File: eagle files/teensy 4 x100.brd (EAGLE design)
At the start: 94.9 x 68.9 mm, 57 parts, among them IC2 LTV846S, IC3 LTV846S, IC4 74AHCT541A, IC5 74AHCT541A, IC6 LM358D, IC7 ULN2003AD

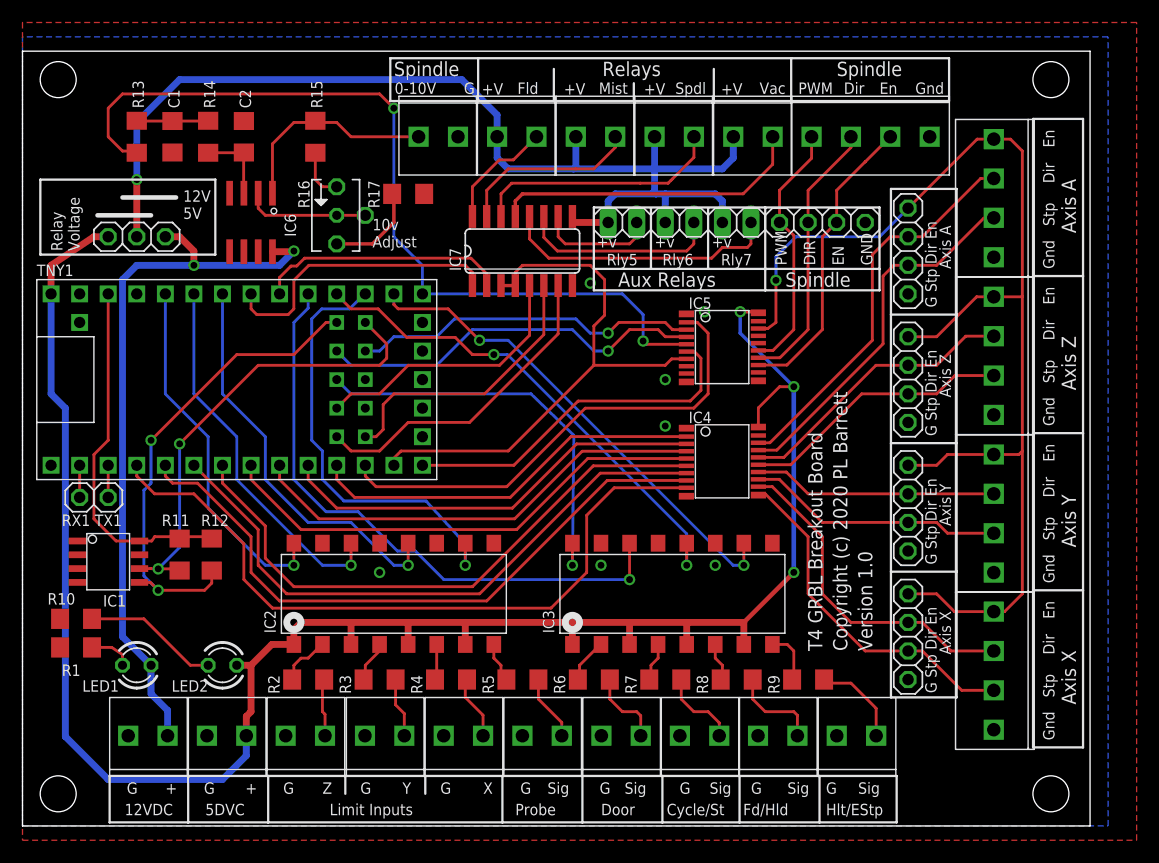
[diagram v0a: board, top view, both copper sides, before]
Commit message: Add files via upload
fix to stepper enable lines
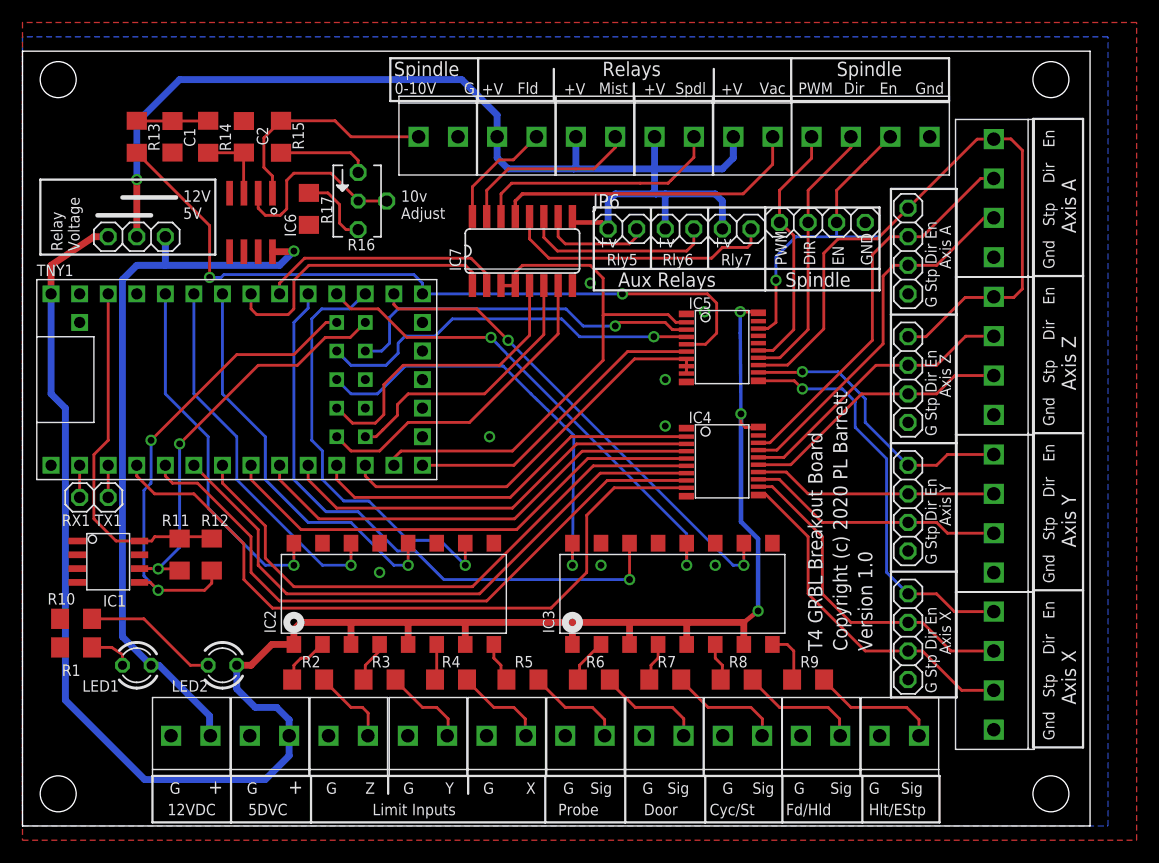
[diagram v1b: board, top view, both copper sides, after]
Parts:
- IC1: value (none) -> 24LCxxx
- JP6: device pinhead:1X06 -> phils connectors:1X06
- moved R17 8.93 mm to (25.5, 54.9), turned to 90 degrees
- moved TR10 3.81 mm to (29.0, 8.02)
- moved TR2 3.81 mm to (22.0, 8.02)
- moved TR5 3.81 mm to (64.0, 8.02)
- moved TR6 3.81 mm to (57.0, 8.02)
- moved TR1 3.81 mm to (15.0, 8.02)
- moved TR7 3.81 mm to (50.0, 8.02)
- moved TR8 3.81 mm to (43.0, 8.02)
- moved TR9 3.81 mm to (36.0, 8.02)
- moved TR3 3.81 mm to (78.0, 8.02)
- moved TR4 3.81 mm to (71.0, 8.02)
- moved R15 3.05 mm to (23.0, 61.3)
- moved R16 2.29 mm to (29.8, 55.6)
- moved JP6 0.57 mm to (58.4, 53.1)
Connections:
- removed net STENO: IC5.P$18, JP1.4, JP2.4, JP4.4, JP8.4, TR11.P$1, TR12.P$1, TR13.P$1, TR20.P$1
- new net STENOX: IC5.P$11, JP1.4, TR11.P$1
- new net STENOY: IC5.P$12, JP2.4, TR12.P$1
- new net STENOZA: IC5.P$13, JP4.4, JP8.4, TR13.P$1, TR20.P$1
- net SPEN: now also IC5.P$2; no longer IC5.P$7
- net SPENO: now also IC5.P$18; no longer IC5.P$13
- net STEN: now also IC5.P$7, IC5.P$8, IC5.P$9; no longer IC5.P$2
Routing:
- net STENO: track 107.4 -> 0.00 mm, vias 1 -> 0
- net STENOZA: track 0.00 -> 60.5 mm
- net STENOX: track 0.00 -> 36.7 mm, vias 0 -> 1
- net STENOY: track 0.00 -> 26.0 mm, vias 0 -> 1
- net SPWM: track 76.4 -> 66.3 mm
- net N$23: track 11.1 -> 17.1 mm
- net STEN: track 43.0 -> 37.1 mm
- net SCL: track 41.0 -> 36.5 mm
- net SPDI: track 31.9 -> 27.7 mm
- net N$22: track 4.56 -> 8.22 mm
- net N$35: track 8.13 -> 11.4 mm
- net N$33: track 7.14 -> 10.2 mm
- net N$31: track 5.86 -> 8.85 mm
- net N$32: track 6.88 -> 9.67 mm
- net RLY5: track 24.2 -> 26.9 mm
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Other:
- board text added: "Cyc/St"
- board text removed: "Cycle/St"

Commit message: Add files via upload
Added i2c header, trace clean up.
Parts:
- added C3, C4: 100n, rcl:C1206
- added JP10: JUMPER-SMT_3_NO_SILK, phils connectors:SMT-JUMPER_3_NO_SILK
- added JP9: (no value), phils connectors:1X05
- moved R13 19.8 mm to (29.2, 55.9)
- moved C1 19.5 mm to (32.1, 55.9)
- moved R14 15.6 mm to (32.1, 61.3), turned to 90 degrees
- moved R16 15.5 mm to (15.6, 61.6), turned to 0 degrees
- moved C2 9.40 mm to (29.1, 61.3), turned to 270 degrees
- moved LED2 9.03 mm to (8.83, 13.1), turned to 270 degrees
- moved IC6 8.69 mm to (24.3, 61.4), turned to 0 degrees
- moved R1 7.82 mm to (5.08, 8.06), turned to 90 degrees
- moved R12 7.59 mm to (13.2, 17.5), turned to 0 degrees
- moved R15 6.88 mm to (22.5, 54.4)
- moved LED1 6.53 mm to (8.95, 7.87), turned to 270 degrees
- moved R10 5.03 mm to (5.08, 13.4), turned to 270 degrees
- moved R11 4.38 mm to (13.2, 19.8), turned to 0 degrees
- moved IC1 4.02 mm to (6.35, 19.7)
- moved IC4 1.80 mm to (61.0, 30.8)
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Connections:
- new net KPSTR: JP10.3, JP9.2
- new net P33: JP10.2, TNY1.33
- net +5V: now also C3.1, C4.1
- net 3.3V: now also JP9.1
- net GND: now also C3.2, C4.2, JP9.5
- net RLY7: now also JP10.1; no longer TNY1.33
- net SCL: now also JP9.4
- net SDA: now also JP9.3
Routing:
- net SPWM: track 66.3 -> 41.6 mm
- net +12V: track 65.0 -> 87.9 mm, vias 1 -> 0
- net KPSTR: track 0.00 -> 16.1 mm
- net P33: track 0.00 -> 15.1 mm, vias 0 -> 1
- net SDA: track 43.1 -> 57.9 mm, vias 2 -> 0
- net RLY7: track 28.8 -> 43.6 mm, vias 0 -> 1
- net SCL: track 36.5 -> 48.0 mm
- net +5V: track 174.1 -> 184.6 mm
- net N$2: track 12.0 -> 3.82 mm
- net N$24: track 6.70 -> 14.2 mm
- net N$22: track 8.22 -> 15.1 mm
- net 3.3V: track 33.1 -> 38.6 mm
- net LIMZ: track 32.3 -> 36.0 mm
- net STEN: track 37.1 -> 33.6 mm
- net N$21: track 6.79 -> 10.3 mm
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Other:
- board text added: "+V St SD SC G"
- board text added: "0-10v Adjust"
- board text added: "3.3V"
- board text added: "I2C"
- board text added: "I2C (def)"
- board text added: "RX"
- board text added: "Relay 7"
- board text added: "TX"
- board text removed: "10v Adjust"
- board text removed: "RX1 TX1"

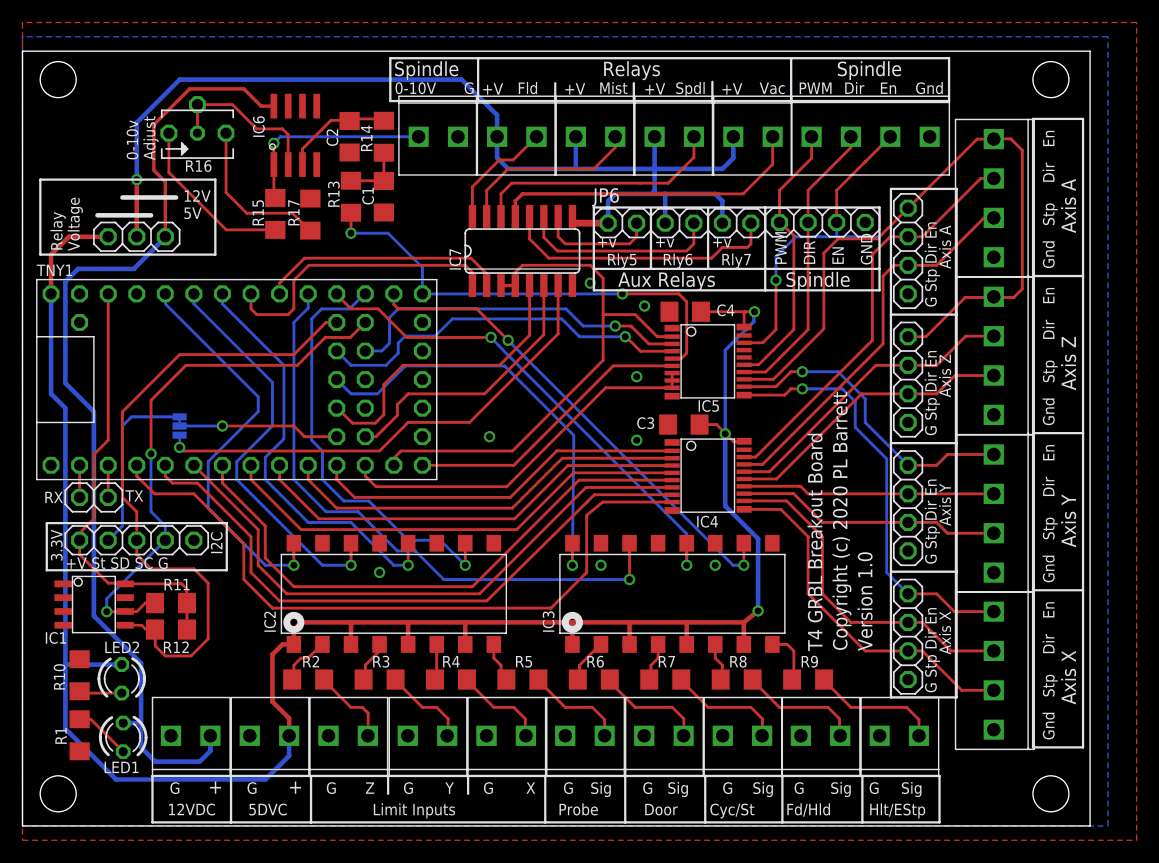
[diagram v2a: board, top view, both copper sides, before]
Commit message: Add files via upload
Changed spindle pin assignments, in line with the Teensy 4 Pinouts PDF
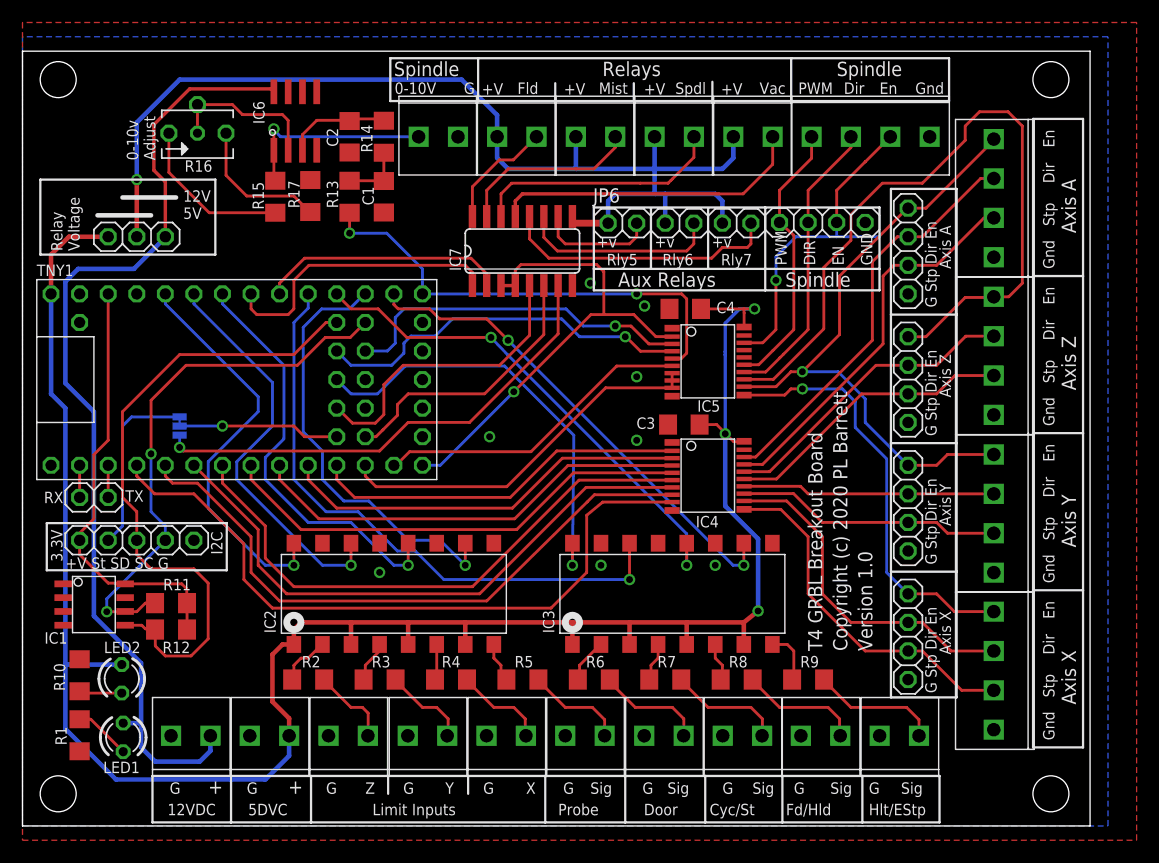
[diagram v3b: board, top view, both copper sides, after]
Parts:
- moved R17 1.65 mm to (25.6, 56.0)
- moved R15 1.52 mm to (22.5, 55.9)
- moved IC6 1.27 mm to (24.3, 62.7)
- moved C4 0.25 mm to (58.9, 46.0)
- moved R13 0.13 mm to (29.1, 55.9)
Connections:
- removed net STENOY: IC5.P$12, JP2.4, TR12.P$1
- removed net STENOZA: IC5.P$13, JP4.4, JP8.4, TR13.P$1, TR20.P$1
- new net STENOYA: IC5.P$12, JP2.4, JP8.4, TR12.P$1, TR20.P$1
- new net STENOZ: IC5.P$13, JP4.4, TR13.P$1
- net SPDI: now also TNY1.11; no longer TNY1.12
- net SPEN: now also TNY1.12; no longer TNY1.11
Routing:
- net STENOZ: track 0.00 -> 66.5 mm
- net STENOZA: track 62.3 -> 0.00 mm
- net STENOYA: track 0.00 -> 56.6 mm, vias 0 -> 1
- net STENOY: track 27.9 -> 0.00 mm, vias 1 -> 0
- net SPEN: track 48.1 -> 43.3 mm, vias 0 -> 1
- net SPDI: track 25.9 -> 28.4 mm
- net N$24: track 14.2 -> 12.6 mm
- net +5V: track 184.6 -> 185.9 mm
- net N$22: track 15.1 -> 14.4 mm
- net PRB: track 38.2 -> 38.8 mm
- net N$23: track 14.4 -> 13.8 mm
- net N$21: track 10.3 -> 9.75 mm
- net +12V: track 87.9 -> 87.3 mm
